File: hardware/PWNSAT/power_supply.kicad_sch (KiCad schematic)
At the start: 32 parts, among them U3 EA3059

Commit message: feat(Hw): Added_BOM
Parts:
- C46, C47, C54, C55: LCSC# (none) -> C140782
- C56, C57, C66: LCSC# (none) -> C77020
- C67, C68, C71, C72: LCSC# (none) -> C327000
- C69, C70, C73, C74: LCSC# (none) -> C415703
- L2, L3, L8, L9: LCSC# (none) -> C7427193
- R10, R28, R30, R4, R40, R68, R70: LCSC# (none) -> C844674
- R51, R67, R69: LCSC# (none) -> C364966
- R61: LCSC# (none) -> C365024
- R64: MANUFACTURER (none) -> ERJ-2RKF1103X
- U3: LCSC# (none) -> C111586

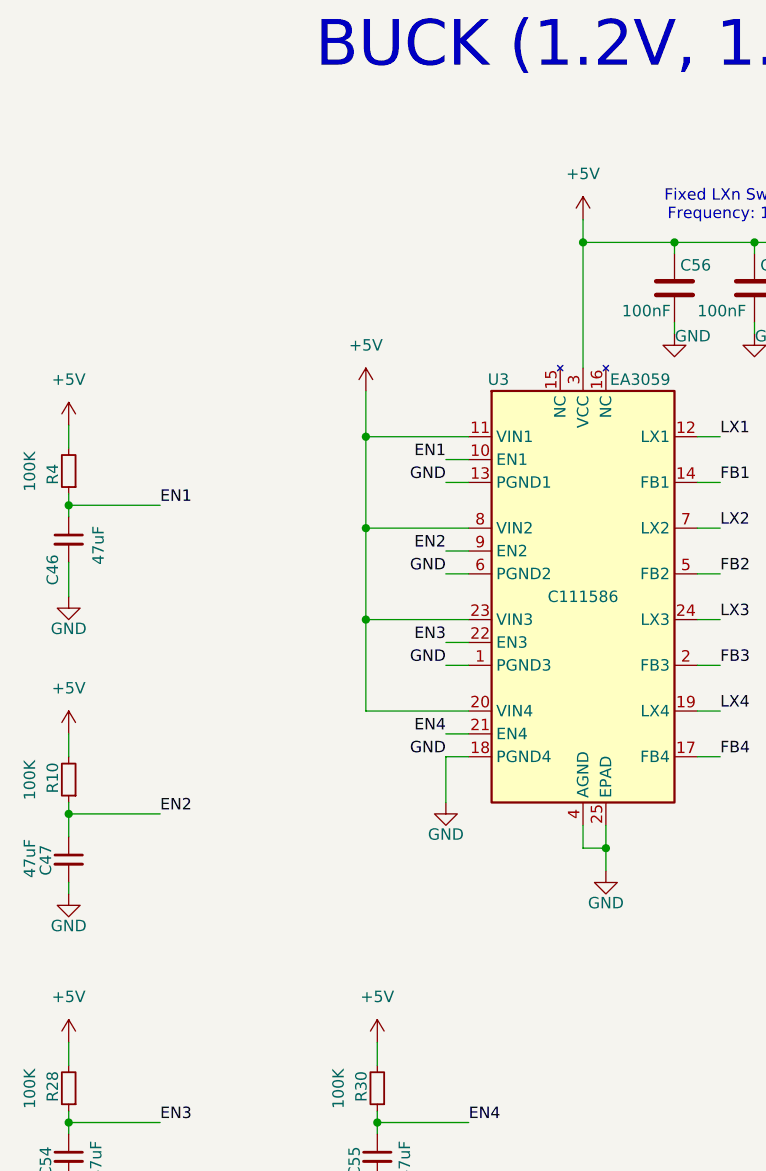
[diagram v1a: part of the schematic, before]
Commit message: feat(Hw):Sch_Updated
Pending_Sensor_Connector
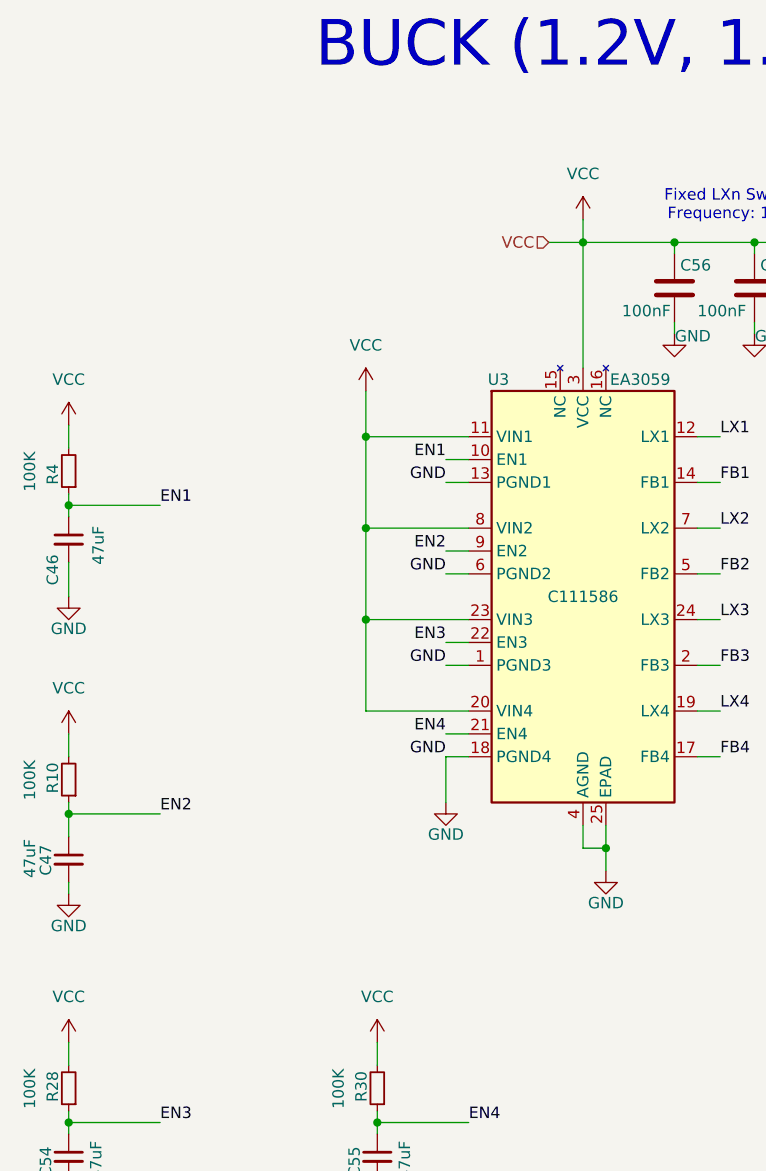
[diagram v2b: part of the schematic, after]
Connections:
- net +5V renamed VCC

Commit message: feat(Hw):Init_Floorplan
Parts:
- renumbered C68 to C31, C70 to C32, C72 to C33, C74 to C34, C56 to C35, C57 to C36, C66 to C37, C46 to C38, C67 to C39, C69 to C40, C71 to C41, C73 to C42, C47 to C43, C54 to C44, C55 to C45, L3 to L1, L9 to L2, L2 to L3, L8 to L4, R61 to R14, R69 to R15, R64 to R16, R70 to R17, R4 to R18, R40 to R19, R67 to R20, R10 to R21, R51 to R22, R68 to R23, R28 to R24, R30 to R25

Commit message: feat(Hw):Update_Battery_Sch_And_Sensors_And_PWNCube
pending_Outputs_connectors
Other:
- company: (none) -> Electronic Cats
- title: (none) -> PWNCube
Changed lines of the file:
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@@
 	(generator_version "9.0")
 	(paper "A4")
+	(title_block
+		(title "PWNCube")
+		(date "2026-01-23")
+		(rev "1.0")
+		(company "Electronic Cats")
+		(comment 1 "Edgar Capuchino")
+	)
 	(text "BUCK (1.2V, 1.8V, 3.3V)"
 		(exclude_from_sim no)

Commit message: feat(Hw):BoM´s_Updated
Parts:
- C32, C34, C40, C42: value 22uf -> 22uF; footprint Capacitor_SMD:C_0402_1005Metric_Pad0.74x0.62mm_HandSolder -> Capacitor_SMD:C_0402_1005Metric; Mnfr# GRM155R60J226ME11D -> (none)
- C35, C36, C37: LCSC# C77020 -> C56392
- R16: LCSC# (none) -> C854086
